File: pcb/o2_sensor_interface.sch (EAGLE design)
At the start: 23 parts, among them IC1 MAX31855KASA+T, U1 IRLB8721PBF, U2 L7805CV, U3 TLV2462CP, X1 22-23-2021

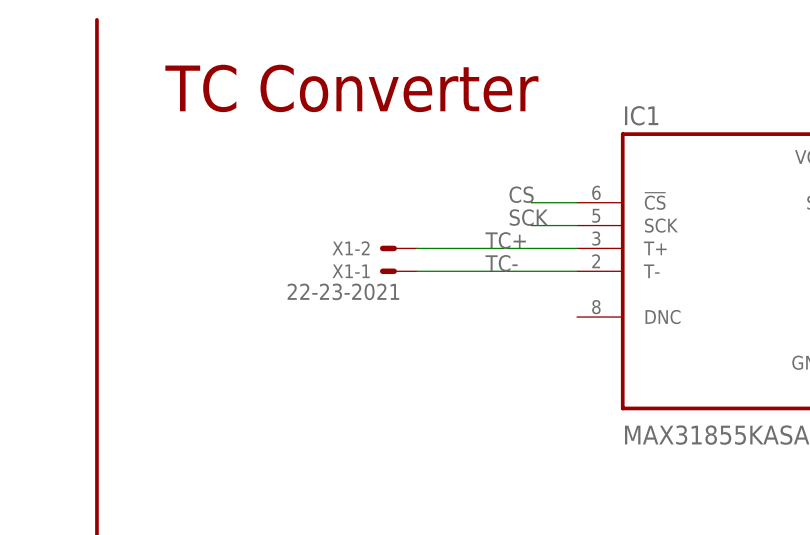
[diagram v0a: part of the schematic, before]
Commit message: added tc connection socket
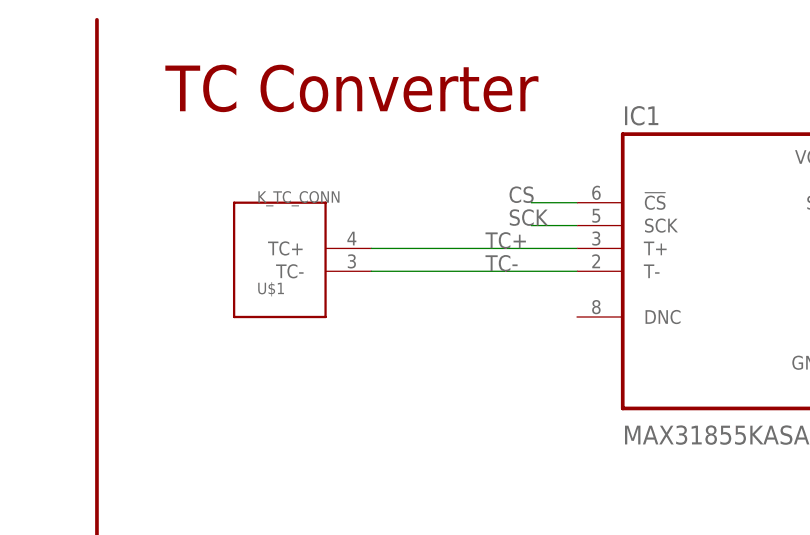
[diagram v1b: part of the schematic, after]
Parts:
- removed X1: 22-23-2021, con-molex:22-23-2021
- added U$1: K_TC_CONN, samdg:K_TC_CONN
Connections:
- net TC+: now also U$1.TC+; no longer X1-2.S
- net TC-: now also U$1.TC-; no longer X1-1.S
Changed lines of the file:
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@@
 <part name="R6" library="adafruit" library_urn="urn:adsk.eagle:library:420" deviceset="R-US_" device="0207/9" package3d_urn="urn:adsk.eagle:package:6240935/1" value="100k"/>
 <part name="IC1" library="MAX31855KASA_T" deviceset="MAX31855KASA+T" device=""/>
-<part name="X1" library="con-molex" library_urn="urn:adsk.eagle:library:165" deviceset="22-23-2021" device="" package3d_urn="urn:adsk.eagle:package:8078633/1"/>
 <part name="C1" library="adafruit" library_urn="urn:adsk.eagle:library:420" deviceset="C-US" device="025-030X050" package3d_urn="urn:adsk.eagle:package:6240322/1" value=".1uF"/>
 <part name="C2" library="adafruit" library_urn="urn:adsk.eagle:library:420" deviceset="C-US" device="025-030X050" package3d_urn="urn:adsk.eagle:package:6240322/1" value="1uF"/>
 <part name="C5" library="adafruit" library_urn="urn:adsk.eagle:library:420" deviceset="CPOL-US" device="E2-4" package3d_urn="urn:adsk.eagle:package:6240495/1" value="10uF"/>
 <part name="FRAME1" library="frames" library_urn="urn:adsk.eagle:library:229" deviceset="FRAME_A_L" device=""/>
+<part name="U$1" library="samdg" deviceset="K_TC_CONN" device=""/>
 </parts>
 <sheets>
@@
 <attribute name="VALUE" x="198.12" y="163.64" size="2.0828" layer="96" ratio="10" rot="SR0"/>
 </instance>
-<instance part="X1" gate="-1" x="172.72" y="182.88" smashed="yes" rot="R180">
-<attribute name="NAME" x="170.18" y="183.642" size="1.524" layer="95" rot="R180"/>
-<attribute name="VALUE" x="173.482" y="181.483" size="1.778" layer="96" rot="R180"/>
-</instance>
-<instance part="X1" gate="-2" x="172.72" y="185.42" smashed="yes" rot="R180">
-<attribute name="NAME" x="170.18" y="186.182" size="1.524" layer="95" rot="R180"/>
-</instance>
 <instance part="C1" gate="G$1" x="254" y="193.04" smashed="yes">
 <attribute name="NAME" x="255.016" y="193.675" size="1.778" layer="95"/>
@@
 <attribute name="SHEET" x="259.08" y="1.27" size="2.54" layer="94"/>
 <attribute name="DRAWING_NAME" x="190.5" y="19.05" size="2.54" layer="94"/>
+</instance>
+<instance part="U$1" gate="A" x="160.02" y="185.42" smashed="yes">
+<attribute name="VALUE" x="157.48" y="190.5" size="1.27" layer="96"/>
+<attribute name="NAME" x="157.48" y="180.34" size="1.27" layer="95"/>
 </instance>
 </instances>
@@
 <segment>
 <pinref part="IC1" gate="G$1" pin="T+"/>
-<wire x1="193.04" y1="185.42" x2="175.26" y2="185.42" width="0.1524" layer="91"/>
+<wire x1="193.04" y1="185.42" x2="170.18" y2="185.42" width="0.1524" layer="91"/>
 <label x="182.88" y="185.42" size="1.778" layer="95"/>
-<pinref part="X1" gate="-2" pin="S"/>
+<pinref part="U$1" gate="A" pin="TC+"/>
 </segment>
 </net>
@@
 <segment>
 <pinref part="IC1" gate="G$1" pin="T-"/>
-<wire x1="193.04" y1="182.88" x2="175.26" y2="182.88" width="0.1524" layer="91"/>
+<wire x1="193.04" y1="182.88" x2="170.18" y2="182.88" width="0.1524" layer="91"/>
 <label x="182.88" y="182.88" size="1.778" layer="95"/>
-<pinref part="X1" gate="-1" pin="S"/>
-</segment>
-</net>
+<pinref part="U$1" gate="A" pin="TC-"/>
+</segment>
+</net>
